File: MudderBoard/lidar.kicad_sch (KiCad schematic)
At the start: 0 parts

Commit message: Component Sorting
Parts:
- added C1, C2: 2.2uF, GRM188R6YA225MA12D:CAPC1608X90N, symbol GRM188R6YA225MA12D:GRM188R6YA225MA12D
- added C3, C4, C7: 4.7uF, TAJB_AVX, symbol TAJB475K035RNJ:TAJB475K035RNJ
- added C5: 2.7nF, GCM188R71C274KA37D:CAPC1608X90N, symbol GCM188R71C274KA37D:GCM188R71C274KA37D
- added C6: CL21B474KAFNNNG, CAP_CL_21_SAM, symbol CL21B474KAFNNNG:CL21B474KAFNNNG
- added L1: 26uH, SD6030, symbol SD6030_270_R:SD6030-270-R
- added R1: 74.1k, RN73R1JTTD7412B25:RESC1608X55N, symbol RN73R1JTTD7412B25:RN73R1JTTD7412B25
- added R2: 7.5k, RC0603N_YAG, symbol RC0603FR_077K5L:RC0603FR-077K5L
- added R3: 43m, RLP73M2BR043JTD:RESC3115X65N, symbol RLP73M2BR043JTD:RLP73M2BR043JTD
- added R4: 21k, RMCF0402FT21K0:RESC1005X35N, symbol RMCF0402FT21K0:RMCF0402FT21K0
- added R5: 14k, RC0402N_YAG, symbol RC0402FR-0714KL:RC0402FR-0714KL
- added R6: 49.3k, RT0603DRE0749K3L:RESC1608X55N, symbol RT0603DRE0749K3L:RT0603DRE0749K3L
- added U1: LM51231QRGRRQ1, RGR0020C-IPC_A, symbol LM51231QRGRRQ1:LM51231QRGRRQ1
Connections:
- new net: C7.1, U1.9 (VCC)
- new net: R1.2, R2.1, U1.13 (UVLO_EN)
- new net: R6.1, U1.15 (RT)
- new net: C6.1, R4.1, U1.16 (VREF_RANGE)
- new net: C5.1, U1.17 (SS)
- new net: R4.2, R5.1, U1.18 (TRK)
- new net: L1.1, R3.2, U1.2 (CSN)
- new net: L1.2, U1.6 (SW)
- new net +24V: C1.1, C2.1, C3.1, C4.1, U1.3 (VOUT_SENSE)
- new net GND: C1.2, C2.2, C3.2, C4.2, C5.2, C6.2, C7.2, R2.2, R5.2, R6.2
- new net VCC: R1.1, R3.1, U1.1 (CSP), U1.12 (MODE), U1.8 (BIAS)

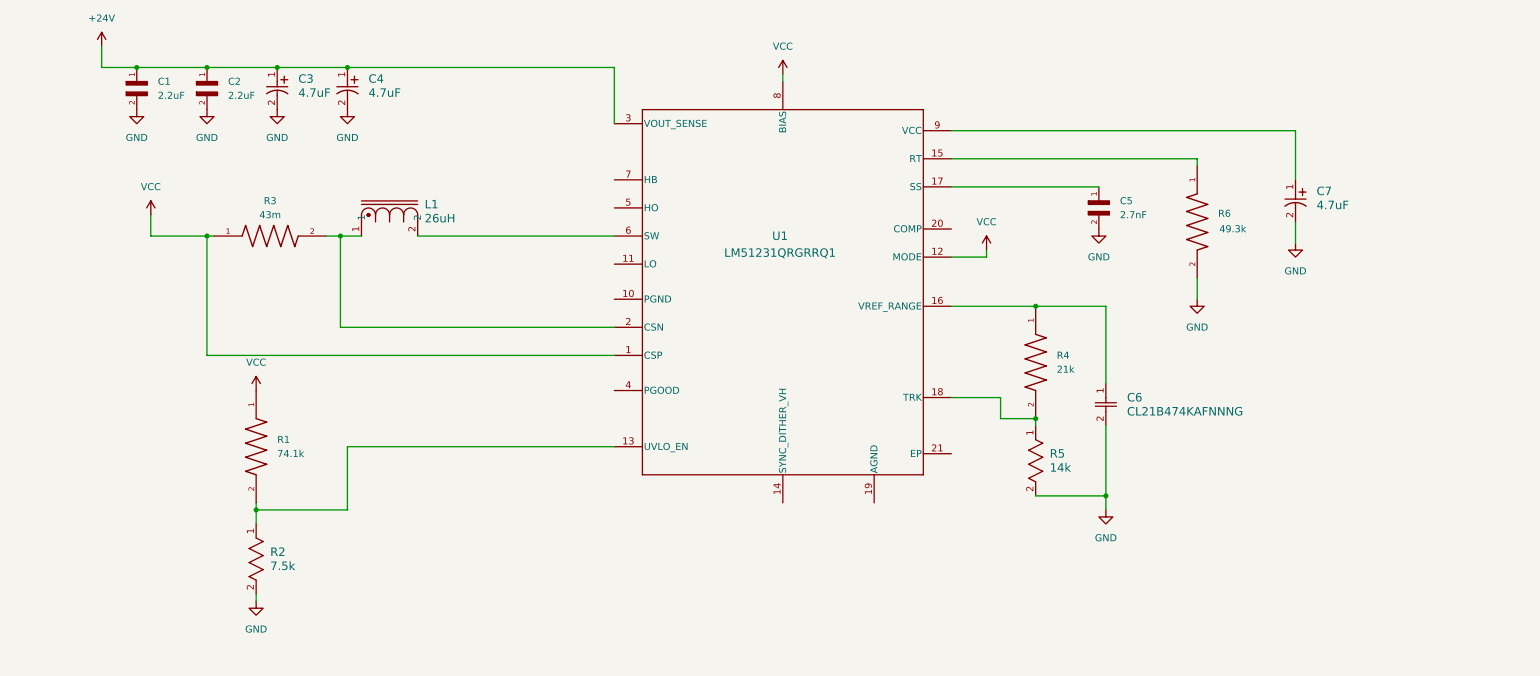
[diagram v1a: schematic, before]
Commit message: mosfet selection LiDar
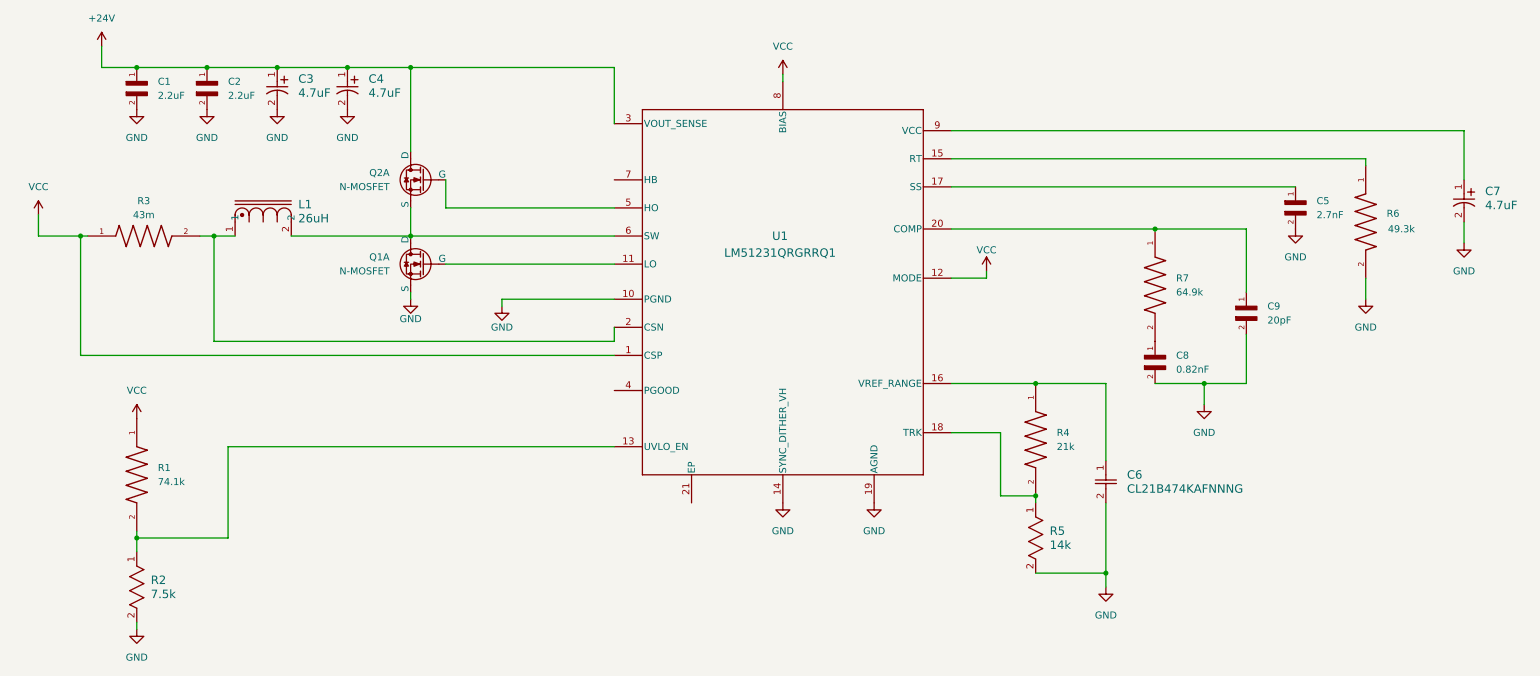
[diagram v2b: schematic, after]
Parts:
- added C8: 0.82nF, GRM033R71E821KA01D:CAPC0603X33N, symbol GRM033R71E821KA01D:GRM033R71E821KA01D
- added C9: 20pF, GRM0335C1H200JA01D:CAPC0603X33N, symbol GRM0335C1H200JA01D:GRM0335C1H200JA01D
- added Q1, Q2: N-MOSFET, symbol DI110N04PQ-AQ:nMOS
- added R7: 64.9k, RC0603FR-0764K9L:RESC1608X55N, symbol RC0603FR-0764K9L:RC0603FR-0764K9L
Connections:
- net +24V: now also Q2.3 (D)
- net GND: now also U1.10 (PGND), U1.14 (SYNC_DITHER_VH), U1.19 (AGND), C8.2, C9.2, Q1.2 (S)
- net at U1.11 (LO): now also Q1.1 (G)
- net at U1.20 (COMP): now also C9.1, R7.1
- net at U1.5 (HO): now also Q2.1 (G)
- net at L1.2, U1.6 (SW): now also Q1.3 (D), Q2.2 (S)
- new net: C8.1, R7.2
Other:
- moved on the sheet: C5, C6, C7, L1, R1, R2, R3, R4, R5, R6

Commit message: Lidar edits
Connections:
- net GND: now also U1.21 (EP)
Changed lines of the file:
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@@
+	(symbol
+		(lib_id "power:GND")
+		(at 134.62 113.03 0)
+		(mirror y)
+		(unit 1)
+		(exclude_from_sim no)
+		(in_bom yes)
+		(on_board yes)
+		(dnp no)
+		(fields_autoplaced yes)
+		(property "Reference" "#PWR020"
+			(at 134.62 119.38 0)
+			(effects
+				(font
+					(size 1.27 1.27)
+				)
+				(hide yes)
+			)
+		)
+		(property "Value" "GND"
+			(at 134.62 118.11 0)
+			(effects
+				(font
+					(size 1.27 1.27)
+				)
+			)
+		)
+		(property "Footprint" ""
+			(at 134.62 113.03 0)
+			(effects
+				(font
+					(size 1.27 1.27)
+				)
+				(hide yes)
+			)
+		)
+		(property "Datasheet" ""
+			(at 134.62 113.03 0)
+			(effects
+				(font
+					(size 1.27 1.27)
+				)
+				(hide yes)
+			)
+		)
+		(property "Description" "Power symbol creates a global label with name \"GND\" , ground"
+			(at 134.62 113.03 0)
+			(effects
+				(font
+					(size 1.27 1.27)
+				)
+				(hide yes)
+			)
+		)
+		(pin "1"
+		)
+		(instances
+			(project "MudderBoard"
+				(path "/cdf98bf7-80ce-4b13-b655-e6c7c589c122/86bd7edb-9c3d-421e-84f7-984954447f61"
+					(reference "#PWR020")
+					(unit 1)
+				)
+			)
+		)
+	)
 	(symbol
 		(lib_id "power:GND")

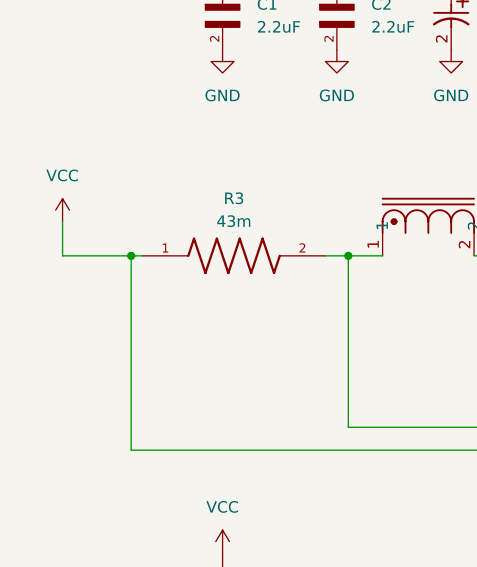
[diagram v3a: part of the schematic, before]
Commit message: note on input cap
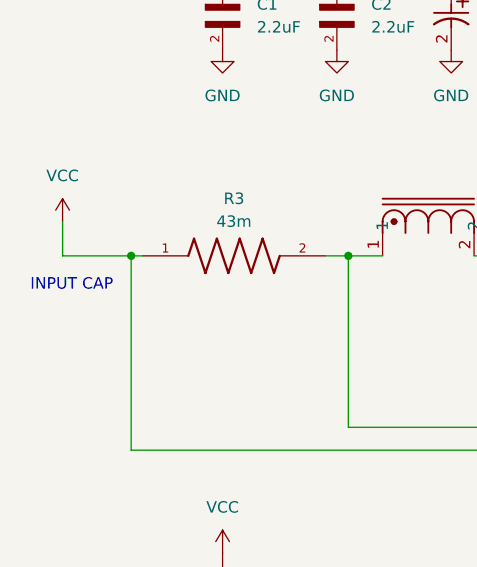
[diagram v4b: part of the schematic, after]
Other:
- note added: "INPUT CAP"
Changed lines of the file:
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@@
+		)
+	)
+	(text "INPUT CAP"
+		(exclude_from_sim no)
+		(at 17.526 68.072 0)
+		(effects
+			(font
+				(size 1.27 1.27)
+			)
 		)
 	)
